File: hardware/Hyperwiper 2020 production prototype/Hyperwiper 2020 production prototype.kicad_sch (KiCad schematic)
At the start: 22 parts, among them J1 Conn_01x05, J2 USB_B, Q2 2N3904, Q3 IRF4905, SW1 SW_DPDT_x2, SW2 SW_Reed, U1 Teensy4.0, U3 Voltage regulator

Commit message: Updated board
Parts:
- J2: footprint Connector_USB:USB_Micro-B_Amphenol_10103594-0001LF_Horizontal -> digikey-footprints:USB_Micro_B_Male_UJ2-MIBH-4-SMT-TR; symbol Connector:USB_B -> dk_USB-DVI-HDMI-Connectors:UJ2-MIBH-4-SMT-TR; Category (none) -> Connectors, Interconnects; DK_Datasheet_Link (none) -> https://www.cui.com/product/resource/digikeypdf/uj2-mibh-4-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; DK_Detail_Page (none) -> /product-detail/en/cui-inc/UJ2-MIBH-4-SMT-TR/102-4006-1-ND/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; Digi-Key_PN (none) -> 102-4006-1-ND; Family (none) -> USB, DVI, HDMI Connectors; MPN (none) -> UJ2-MIBH-4-SMT-TR; Manufacturer (none) -> CUI Inc.; Status (none) -> Active
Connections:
- net GND: now also J2.5; no longer J2.4 (GND)
- net at U1.53 (D-): now also J2.4; no longer J2.2 (D-)
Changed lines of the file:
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@@
     (stroke (width 0) (type solid) (color 0 0 0 0))
   )
-  (wire (pts (xy 107.95 25.4) (xy 120.015 25.4))
-    (stroke (width 0) (type solid) (color 0 0 0 0))
-  )
-  (wire (pts (xy 107.95 27.94) (xy 120.015 27.94))
+  (wire (pts (xy 107.95 25.4) (xy 123.19 29.845))
+    (stroke (width 0) (type solid) (color 0 0 0 0))
+  )
+  (wire (pts (xy 107.95 27.94) (xy 123.19 32.385))
     (stroke (width 0) (type solid) (color 0 0 0 0))
   )
@@
     (stroke (width 0) (type solid) (color 0 0 0 0))
   )
-  (wire (pts (xy 116.84 20.32) (xy 116.84 81.28))
-    (stroke (width 0) (type solid) (color 0 0 0 0))
-  )
   (wire (pts (xy 116.84 81.28) (xy 107.95 81.28))
     (stroke (width 0) (type solid) (color 0 0 0 0))
   )
-  (wire (pts (xy 120.015 20.32) (xy 116.84 20.32))
+  (wire (pts (xy 120.015 24.765) (xy 116.84 81.28))
+    (stroke (width 0) (type solid) (color 0 0 0 0))
+  )
+  (wire (pts (xy 121.92 34.925) (xy 121.92 37.465))
+    (stroke (width 0) (type solid) (color 0 0 0 0))
+  )
+  (wire (pts (xy 123.19 24.765) (xy 120.015 24.765))
+    (stroke (width 0) (type solid) (color 0 0 0 0))
+  )
+  (wire (pts (xy 123.19 34.925) (xy 121.92 34.925))
     (stroke (width 0) (type solid) (color 0 0 0 0))
   )
@@
     (pin "1")
   )
-  (symbol (lib_id "power:GND") (at 127.635 35.56 0) (unit 1)
-    (in_bom yes) (on_board yes)
-    (property "Reference" "#PWR0118" (id 0) (at 127.635 41.91 0)
-      (effects (font (size 1.27 1.27)) hide)
-    )
-    (property "Value" "GND" (id 1) (at 130.81 36.83 0))
-    (property "Footprint" "" (id 2) (at 127.635 35.56 0)
-      (effects (font (size 1.27 1.27)) hide)
-    )
-    (property "Datasheet" "" (id 3) (at 127.635 35.56 0)
+  (symbol (lib_id "power:GND") (at 121.92 37.465 0) (unit 1)
+    (in_bom yes) (on_board yes)
+    (property "Reference" "#PWR0118" (id 0) (at 121.92 43.815 0)
+      (effects (font (size 1.27 1.27)) hide)
+    )
+    (property "Value" "GND" (id 1) (at 125.095 38.735 0))
+    (property "Footprint" "" (id 2) (at 121.92 37.465 0)
+      (effects (font (size 1.27 1.27)) hide)
+    )
+    (property "Datasheet" "" (id 3) (at 121.92 37.465 0)
       (effects (font (size 1.27 1.27)) hide)
     )
@@
     (pin "9")
   )
-  (symbol (lib_id "Connector:USB_B") (at 127.635 25.4 0) (mirror y) (unit 1)
-    (in_bom yes) (on_board yes) (fields_autoplaced)
-    (property "Reference" "J2" (id 0) (at 133.4771 26.0361 0)
-      (effects (font (size 1.27 1.27)) (justify right))
-    )
-    (property "Value" "USB_B" (id 1) (at 133.4771 28.3348 0)
-      (effects (font (size 1.27 1.27)) (justify right))
-    )
-    (property "Footprint" "Connector_USB:USB_Micro-B_Amphenol_10103594-0001LF_Horizontal" (id 2) (at 123.825 26.67 0)
-      (effects (font (size 1.27 1.27)) hide)
-    )
-    (property "Datasheet" "https://www.digikey.com/en/products/detail/amphenol-icc-fci/10118194-0001LF/2785389" (id 3) (at 123.825 26.67 0)
-      (effects (font (size 1.27 1.27)) hide)
+  (symbol (lib_id "Relay:SANYOU_SRD_Form_C") (at 268.605 48.895 0) (unit 1)
+    (in_bom yes) (on_board yes)
+    (property "Reference" "RLY1" (id 0) (at 270.51 57.8309 0)
+      (effects (font (size 1.524 1.524)))
+    )
+    (property "Value" "JSM1-12V-5" (id 1) (at 261.62 37.6785 0)
+      (effects (font (size 1.524 1.524)))
+    )
+    (property "Footprint" "Relay_THT:Relay_SPDT_SANYOU_SRD_Series_Form_C" (id 2) (at 280.035 50.165 0)
+      (effects (font (size 1.27 1.27)) (justify left) hide)
+    )
+    (property "Datasheet" "http://www.sanyourelay.ca/public/products/pdf/SRD.pdf" (id 3) (at 268.605 48.895 0)
+      (effects (font (size 1.27 1.27)) hide)
+    )
+    (property "Digi-Key_PN" "255-1240-ND" (id 4) (at 273.685 38.735 0)
+      (effects (font (size 1.524 1.524)) (justify left) hide)
+    )
+    (property "MPN" "JSM1-12V-5" (id 5) (at 273.685 36.195 0)
+      (effects (font (size 1.524 1.524)) (justify left) hide)
+    )
+    (property "Category" "Relays" (id 6) (at 273.685 33.655 0)
+      (effects (font (size 1.524 1.524)) (justify left) hide)
+    )
+    (property "Family" "Automotive Relays" (id 7) (at 273.685 31.115 0)
+      (effects (font (size 1.524 1.524)) (justify left) hide)
+    )
+    (property "DK_Datasheet_Link" "https://media.digikey.com/pdf/Data%20Sheets/Panasonic%20Electric%20Works%20PDFs/JS-M_Series_Rev_Dec_2011.pdf" (id 8) (at 273.685 28.575 0)
+      (effects (font (size 1.524 1.524)) (justify left) hide)
+    )
+    (property "DK_Detail_Page" "/product-detail/en/panasonic-electric-works/JSM1-12V-5/255-1240-ND/274764" (id 9) (at 273.685 26.035 0)
+      (effects (font (size 1.524 1.524)) (justify left) hide)
+    )
+    (property "Description" "RELAY AUTOMOTIVE SPDT 15A 12V" (id 10) (at 273.685 23.495 0)
+      (effects (font (size 1.524 1.524)) (justify left) hide)
+    )
+    (property "Manufacturer" "Panasonic Electric Works" (id 11) (at 273.685 20.955 0)
+      (effects (font (size 1.524 1.524)) (justify left) hide)
+    )
+    (property "Status" "Active" (id 12) (at 273.685 18.415 0)
+      (effects (font (size 1.524 1.524)) (justify left) hide)
     )
     (pin "1")
@@
     (pin "5")
   )
-  (symbol (lib_id "Relay:SANYOU_SRD_Form_C") (at 268.605 48.895 0) (unit 1)
-    (in_bom yes) (on_board yes)
-    (property "Reference" "RLY1" (id 0) (at 270.51 57.8309 0)
-      (effects (font (size 1.524 1.524)))
-    )
-    (property "Value" "JSM1-12V-5" (id 1) (at 261.62 37.6785 0)
-      (effects (font (size 1.524 1.524)))
-    )
-    (property "Footprint" "Relay_THT:Relay_SPDT_SANYOU_SRD_Series_Form_C" (id 2) (at 280.035 50.165 0)
-      (effects (font (size 1.27 1.27)) (justify left) hide)
-    )
-    (property "Datasheet" "http://www.sanyourelay.ca/public/products/pdf/SRD.pdf" (id 3) (at 268.605 48.895 0)
-      (effects (font (size 1.27 1.27)) hide)
-    )
-    (property "Digi-Key_PN" "255-1240-ND" (id 4) (at 273.685 38.735 0)
-      (effects (font (size 1.524 1.524)) (justify left) hide)
-    )
-    (property "MPN" "JSM1-12V-5" (id 5) (at 273.685 36.195 0)
-      (effects (font (size 1.524 1.524)) (justify left) hide)
-    )
-    (property "Category" "Relays" (id 6) (at 273.685 33.655 0)
-      (effects (font (size 1.524 1.524)) (justify left) hide)
-    )
-    (property "Family" "Automotive Relays" (id 7) (at 273.685 31.115 0)
-      (effects (font (size 1.524 1.524)) (justify left) hide)
-    )
-    (property "DK_Datasheet_Link" "https://media.digikey.com/pdf/Data%20Sheets/Panasonic%20Electric%20Works%20PDFs/JS-M_Series_Rev_Dec_2011.pdf" (id 8) (at 273.685 28.575 0)
-      (effects (font (size 1.524 1.524)) (justify left) hide)
-    )
-    (property "DK_Detail_Page" "/product-detail/en/panasonic-electric-works/JSM1-12V-5/255-1240-ND/274764" (id 9) (at 273.685 26.035 0)
-      (effects (font (size 1.524 1.524)) (justify left) hide)
-    )
-    (property "Description" "RELAY AUTOMOTIVE SPDT 15A 12V" (id 10) (at 273.685 23.495 0)
-      (effects (font (size 1.524 1.524)) (justify left) hide)
-    )
-    (property "Manufacturer" "Panasonic Electric Works" (id 11) (at 273.685 20.955 0)
-      (effects (font (size 1.524 1.524)) (justify left) hide)
-    )
-    (property "Status" "Active" (id 12) (at 273.685 18.415 0)
+  (symbol (lib_id "dk_USB-DVI-HDMI-Connectors:UJ2-MIBH-4-SMT-TR") (at 130.81 29.845 0) (mirror y) (unit 1)
+    (in_bom yes) (on_board yes) (fields_autoplaced)
+    (property "Reference" "J2" (id 0) (at 136.6521 30.4811 0)
+      (effects (font (size 1.27 1.27)) (justify right))
+    )
+    (property "Value" "USB_B" (id 1) (at 136.6521 32.7798 0)
+      (effects (font (size 1.27 1.27)) (justify right))
+    )
+    (property "Footprint" "digikey-footprints:USB_Micro_B_Male_UJ2-MIBH-4-SMT-TR" (id 2) (at 125.73 24.765 0)
+      (effects (font (size 1.524 1.524)) (justify left) hide)
+    )
+    (property "Datasheet" "https://www.cui.com/product/resource/digikeypdf/uj2-mibh-4-smt.pdf" (id 3) (at 125.73 22.225 0)
+      (effects (font (size 1.524 1.524)) (justify left) hide)
+    )
+    (property "Digi-Key_PN" "102-4006-1-ND" (id 4) (at 125.73 19.685 0)
+      (effects (font (size 1.524 1.524)) (justify left) hide)
+    )
+    (property "MPN" "UJ2-MIBH-4-SMT-TR" (id 5) (at 125.73 17.145 0)
+      (effects (font (size 1.524 1.524)) (justify left) hide)
+    )
+    (property "Category" "Connectors, Interconnects" (id 6) (at 125.73 14.605 0)
+      (effects (font (size 1.524 1.524)) (justify left) hide)
+    )
+    (property "Family" "USB, DVI, HDMI Connectors" (id 7) (at 125.73 12.065 0)
+      (effects (font (size 1.524 1.524)) (justify left) hide)
+    )
+    (property "DK_Datasheet_Link" "https://www.cui.com/product/resource/digikeypdf/uj2-mibh-4-smt.pdf" (id 8) (at 125.73 9.525 0)
+      (effects (font (size 1.524 1.524)) (justify left) hide)
+    )
+    (property "DK_Detail_Page" "/product-detail/en/cui-inc/UJ2-MIBH-4-SMT-TR/102-4006-1-ND/6187928" (id 9) (at 125.73 6.985 0)
+      (effects (font (size 1.524 1.524)) (justify left) hide)
+    )
+    (property "Description" "CONN RCPT USB2.0 MICRO B SMD R/A" (id 10) (at 125.73 4.445 0)
+      (effects (font (size 1.524 1.524)) (justify left) hide)
+    )
+    (property "Manufacturer" "CUI Inc." (id 11) (at 125.73 1.905 0)
+      (effects (font (size 1.524 1.524)) (justify left) hide)
+    )
+    (property "Status" "Active" (id 12) (at 125.73 -0.635 0)
       (effects (font (size 1.524 1.524)) (justify left) hide)
     )
@@
     (pin "4")
     (pin "5")
+    (pin "SH")
   )
   (symbol (lib_id "SparkFun-RF:XBEE") (at 64.135 124.46 0) (unit 1)
@@
     )
     (path "/b2ed6726-d6be-49ad-bfde-2fa1b7fc0736"
-      (reference "J2") (unit 1) (value "USB_B") (footprint "Connector_USB:USB_Micro-B_Amphenol_10103594-0001LF_Horizontal")
+      (reference "J2") (unit 1) (value "USB_B") (footprint "digikey-footprints:USB_Micro_B_Male_UJ2-MIBH-4-SMT-TR")
     )
     (path "/e866b7a7-861f-4eaf-84b8-bf844f4ad0ac"

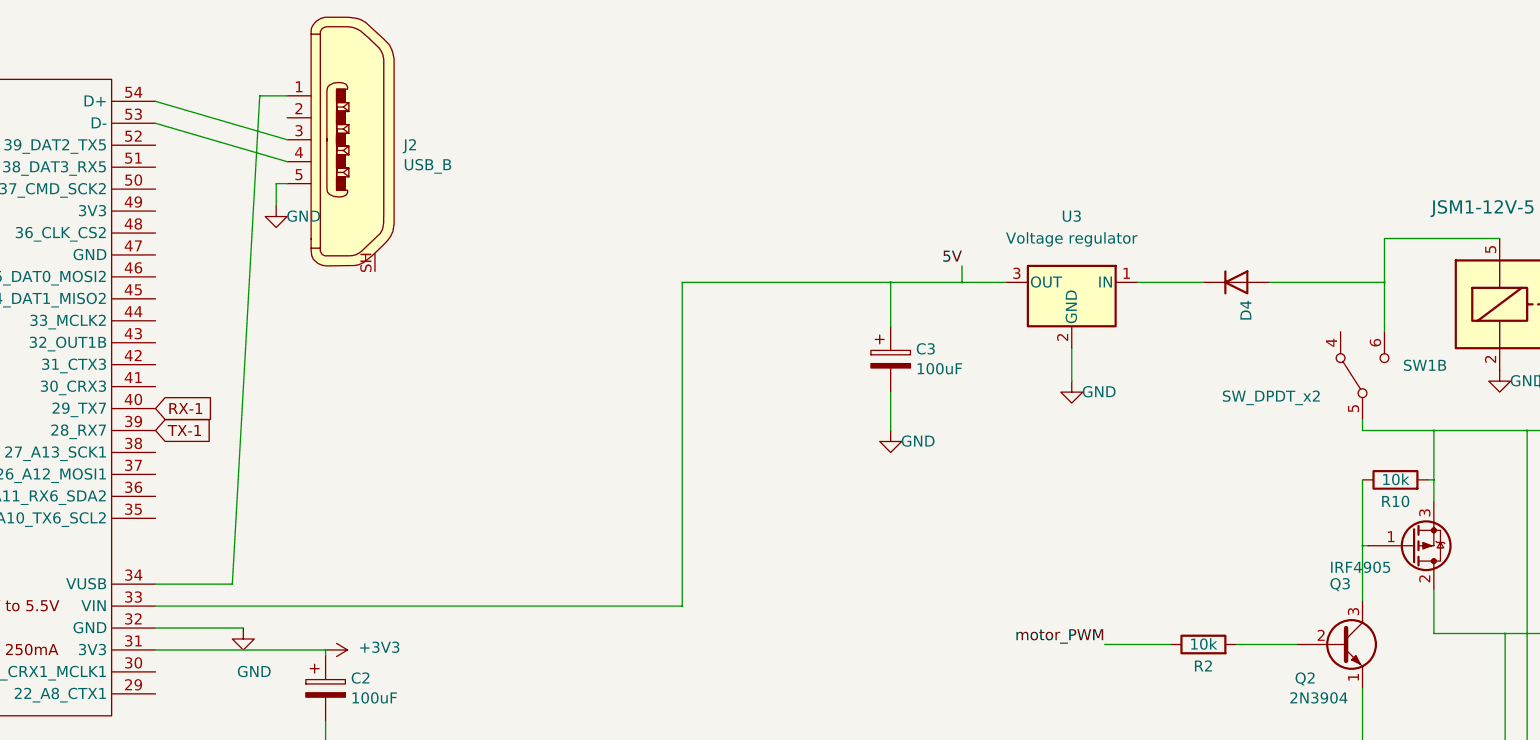
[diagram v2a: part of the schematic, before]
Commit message: updated code for mosfet
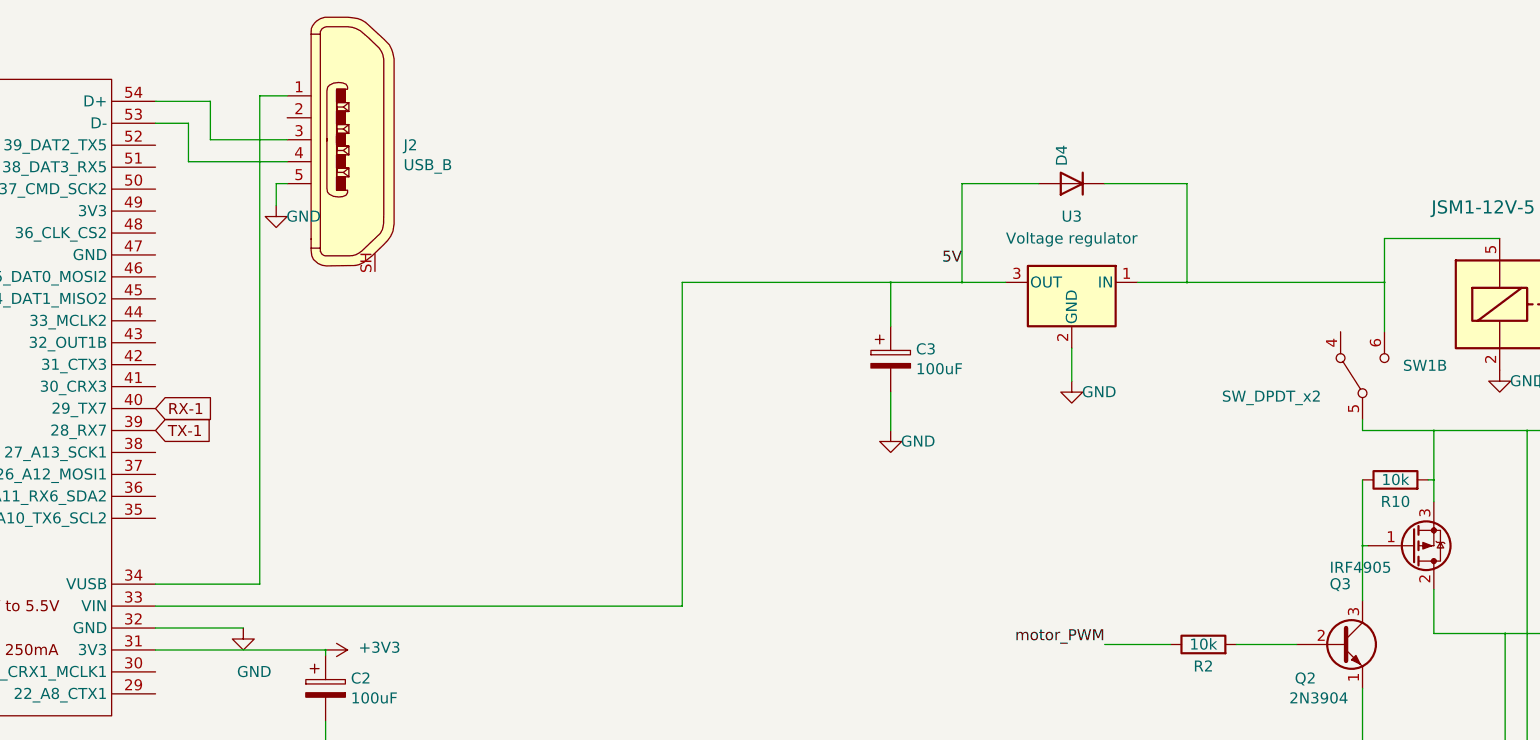
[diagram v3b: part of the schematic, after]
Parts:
- U1: footprint Teensy:Teensy40 -> Hyperwiper 2020 production prototype all:Teensy40
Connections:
- net 5V: now also D4.1 (A)
- net at RLY1.5, SW1.6 (C): now also D4.2 (K), U3.1 (IN); no longer D4.1 (A)
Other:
- moved on the sheet: D4
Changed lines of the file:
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@@
   (junction (at 193.04 46.355) (diameter 0.259) (color 0 0 0 0))
   (junction (at 201.295 46.355) (diameter 0.259) (color 0 0 0 0))
+  (junction (at 227.33 46.355) (diameter 0.259) (color 0 0 0 0))
   (junction (at 241.935 109.855) (diameter 0.259) (color 0 0 0 0))
   (junction (at 241.935 122.555) (diameter 0.259) (color 0 0 0 0))
@@
     (stroke (width 0) (type solid) (color 0 0 0 0))
   )
-  (wire (pts (xy 107.95 25.4) (xy 123.19 29.845))
-    (stroke (width 0) (type solid) (color 0 0 0 0))
-  )
-  (wire (pts (xy 107.95 27.94) (xy 123.19 32.385))
+  (wire (pts (xy 107.95 25.4) (xy 114.3 25.4))
+    (stroke (width 0) (type solid) (color 0 0 0 0))
+  )
+  (wire (pts (xy 107.95 81.28) (xy 120.015 81.28))
     (stroke (width 0) (type solid) (color 0 0 0 0))
   )
@@
     (stroke (width 0) (type solid) (color 0 0 0 0))
   )
-  (wire (pts (xy 116.84 81.28) (xy 107.95 81.28))
-    (stroke (width 0) (type solid) (color 0 0 0 0))
-  )
-  (wire (pts (xy 120.015 24.765) (xy 116.84 81.28))
+  (wire (pts (xy 111.76 27.94) (xy 107.95 27.94))
+    (stroke (width 0) (type solid) (color 0 0 0 0))
+  )
+  (wire (pts (xy 111.76 32.385) (xy 111.76 27.94))
+    (stroke (width 0) (type solid) (color 0 0 0 0))
+  )
+  (wire (pts (xy 114.3 29.845) (xy 114.3 25.4))
+    (stroke (width 0) (type solid) (color 0 0 0 0))
+  )
+  (wire (pts (xy 120.015 81.28) (xy 120.015 24.765))
     (stroke (width 0) (type solid) (color 0 0 0 0))
   )
@@
     (stroke (width 0) (type solid) (color 0 0 0 0))
   )
+  (wire (pts (xy 123.19 29.845) (xy 114.3 29.845))
+    (stroke (width 0) (type solid) (color 0 0 0 0))
+  )
+  (wire (pts (xy 123.19 32.385) (xy 111.76 32.385))
+    (stroke (width 0) (type solid) (color 0 0 0 0))
+  )
   (wire (pts (xy 123.19 34.925) (xy 121.92 34.925))
     (stroke (width 0) (type solid) (color 0 0 0 0))
@@
     (stroke (width 0) (type solid) (color 0 0 0 0))
   )
-  (wire (pts (xy 201.295 44.45) (xy 201.295 46.355))
+  (wire (pts (xy 201.295 34.925) (xy 201.295 46.355))
     (stroke (width 0) (type solid) (color 0 0 0 0))
   )
@@
     (stroke (width 0) (type solid) (color 0 0 0 0))
   )
+  (wire (pts (xy 210.185 34.925) (xy 201.295 34.925))
+    (stroke (width 0) (type solid) (color 0 0 0 0))
+  )
   (wire (pts (xy 213.995 53.975) (xy 213.995 57.785))
     (stroke (width 0) (type solid) (color 0 0 0 0))
   )
+  (wire (pts (xy 217.805 34.925) (xy 227.33 34.925))
+    (stroke (width 0) (type solid) (color 0 0 0 0))
+  )
   (wire (pts (xy 217.805 88.265) (xy 225.425 88.265))
     (stroke (width 0) (type solid) (color 0 0 0 0))
@@
     (stroke (width 0) (type solid) (color 0 0 0 0))
   )
-  (wire (pts (xy 221.615 46.355) (xy 229.235 46.355))
+  (wire (pts (xy 221.615 46.355) (xy 227.33 46.355))
+    (stroke (width 0) (type solid) (color 0 0 0 0))
+  )
+  (wire (pts (xy 227.33 34.925) (xy 227.33 46.355))
+    (stroke (width 0) (type solid) (color 0 0 0 0))
+  )
+  (wire (pts (xy 227.33 46.355) (xy 250.19 46.355))
     (stroke (width 0) (type solid) (color 0 0 0 0))
   )
@@
   )
   (wire (pts (xy 236.22 109.855) (xy 241.935 109.855))
-    (stroke (width 0) (type solid) (color 0 0 0 0))
-  )
-  (wire (pts (xy 236.855 46.355) (xy 250.19 46.355))
     (stroke (width 0) (type solid) (color 0 0 0 0))
   )
@@
     (pin "2")
   )
-  (symbol (lib_id "Simulation_SPICE:DIODE") (at 233.045 46.355 180) (unit 1)
-    (in_bom yes) (on_board yes)
-    (property "Reference" "D4" (id 0) (at 234.1944 48.3871 90)
-      (effects (font (size 1.27 1.27)) (justify left))
-    )
-    (property "Value" "DIODE" (id 1) (at 231.896 48.387 90)
+  (symbol (lib_id "Simulation_SPICE:DIODE") (at 213.995 34.925 0) (unit 1)
+    (in_bom yes) (on_board yes)
+    (property "Reference" "D4" (id 0) (at 212.8456 32.8929 90)
+      (effects (font (size 1.27 1.27)) (justify left))
+    )
+    (property "Value" "DIODE" (id 1) (at 215.144 32.893 90)
       (effects (font (size 1.27 1.27)) (justify left) hide)
     )
-    (property "Footprint" "Diode_THT:D_DO-35_SOD27_P10.16mm_Horizontal" (id 2) (at 233.045 46.355 0)
-      (effects (font (size 1.27 1.27)) hide)
-    )
-    (property "Datasheet" "~" (id 3) (at 233.045 46.355 0)
-      (effects (font (size 1.27 1.27)) hide)
-    )
-    (property "Spice_Netlist_Enabled" "Y" (id 4) (at 233.045 46.355 0)
+    (property "Footprint" "Diode_THT:D_DO-35_SOD27_P10.16mm_Horizontal" (id 2) (at 213.995 34.925 0)
+      (effects (font (size 1.27 1.27)) hide)
+    )
+    (property "Datasheet" "~" (id 3) (at 213.995 34.925 0)
+      (effects (font (size 1.27 1.27)) hide)
+    )
+    (property "Spice_Netlist_Enabled" "Y" (id 4) (at 213.995 34.925 0)
       (effects (font (size 1.27 1.27)) (justify left) hide)
     )
-    (property "Spice_Primitive" "V" (id 5) (at 233.045 46.355 0)
+    (property "Spice_Primitive" "V" (id 5) (at 213.995 34.925 0)
       (effects (font (size 1.27 1.27)) (justify left) hide)
     )
@@
     (property "Reference" "U1" (id 0) (at 80.01 18.7768 0))
     (property "Value" "Teensy4.0" (id 1) (at 78.74 100.33 0))
-    (property "Footprint" "Teensy:Teensy40" (id 2) (at 69.8498 54.6102 0)
+    (property "Footprint" "Hyperwiper 2020 production prototype all:Teensy40" (id 2) (at 69.8498 54.6102 0)
       (effects (font (size 1.27 1.27)) hide)
     )
@@
     )
     (path "/6616c3fb-93b5-47a8-bfa7-91ec7bef9974"
-      (reference "U1") (unit 1) (value "Teensy4.0") (footprint "Teensy:Teensy40")
+      (reference "U1") (unit 1) (value "Teensy4.0") (footprint "Hyperwiper 2020 production prototype all:Teensy40")
     )
     (path "/f9d2509a-a206-4349-9d2a-528f7b1ec6de"
